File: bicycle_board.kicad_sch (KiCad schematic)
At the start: 70 parts, among them J1 Micro_SD_Card, J10 USB_A, J11 Conn_01x04, J12 Conn_01x01, J13 Conn_01x04, J14 Conn_01x01, J2 USB_C_Receptacle_USB2.0_16P, J5 Conn_01x08, J6 Conn_01x04, J7 Conn_01x05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

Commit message: 调整启动相关GPIO，ESO32添加GPIO9上拉电阻；STM32 BOOT0添加下拉电阻
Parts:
- added R6, R7: 10k, Resistor_SMD:R_0402_1005Metric, symbol Device:R
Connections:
- net +3.3V: now also R6.1
- net GND: now also R7.1
- net I2SO_BCK: now also U14.4 (IO5); no longer U14.7 (IO8)
- net I2SO_SD: now also U14.7 (IO8); no longer U14.8 (IO9)
- net I2SO_WS: now also U14.8 (IO9), R6.2; no longer U14.4 (IO5)
- net at U15.44 (BOOT0): now also R7.2
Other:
- note added: "GPIO2,8,9与启动模式有关"
- note added: "TF卡槽处已上拉"

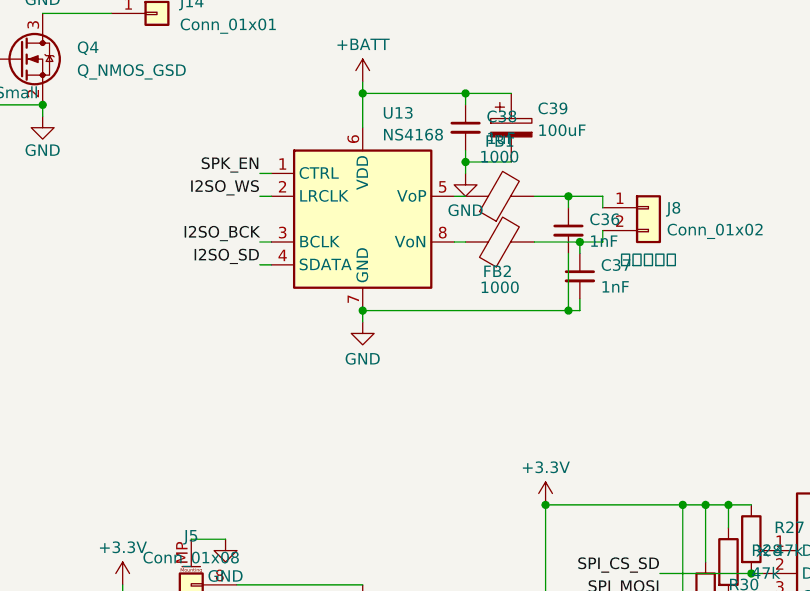
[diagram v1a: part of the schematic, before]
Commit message: 按数据手册调整NS4168布线，电源GND改用单点连接，加粗电源和喇叭走线到0.6mm，中心焊盘连接GND增强散热性能
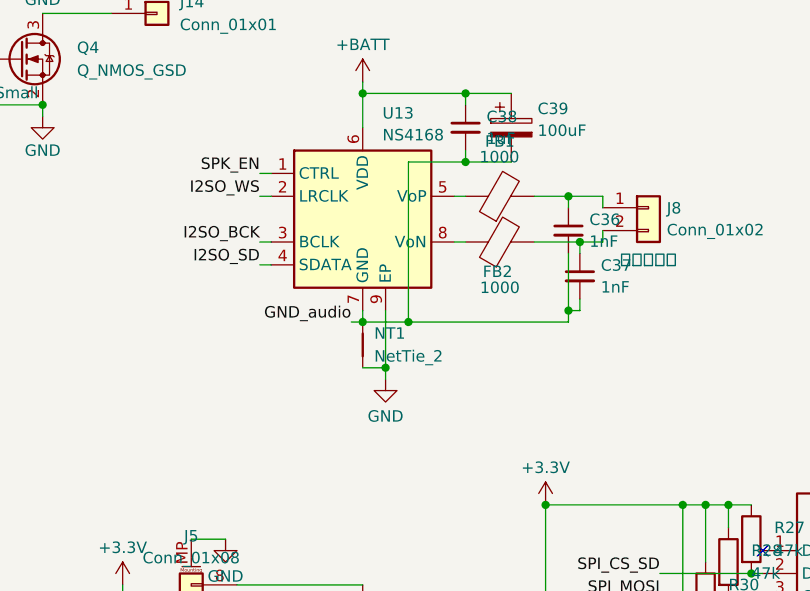
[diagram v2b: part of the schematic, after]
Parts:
- added NT1: NetTie_2, NetTie:NetTie-2_SMD_Pad0.5mm, symbol Device:NetTie_2
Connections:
- net GND: now also U13.9 (EP), NT1.1; no longer C36.2, C37.2, C38.2, C39.2, U13.7 (GND)
- new net GND_audio: C36.2, C37.2, C38.2, C39.2, NT1.2, U13.7 (GND)
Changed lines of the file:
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@@
 	)
 	(junction
+		(at 78.74 143.51)
+		(diameter 0)
+		(color 0 0 0 0)
+	)
+	(junction
 		(at 29.21 97.79)
 		(diameter 0)
@@
 	)
 	(junction
-		(at 73.66 142.24)
+		(at 93.98 176.53)
 		(diameter 0)
 		(color 0 0 0 0)
 	)
 	(junction
-		(at 93.98 176.53)
+		(at 115.57 63.5)
 		(diameter 0)
 		(color 0 0 0 0)
 	)
 	(junction
-		(at 115.57 63.5)
+		(at 232.41 118.11)
 		(diameter 0)
 		(color 0 0 0 0)
 	)
 	(junction
-		(at 232.41 118.11)
+		(at 76.2 148.59)
 		(diameter 0)
 		(color 0 0 0 0)
@@
 	)
 	(junction
-		(at 85.09 125.73)
-		(diameter 0)
-		(color 0 0 0 0)
-	)
-	(junction
 		(at 160.02 35.56)
 		(diameter 0)
@@
 	)
 	(junction
+		(at 85.09 125.73)
+		(diameter 0)
+		(color 0 0 0 0)
+	)
+	(junction
 		(at 161.29 35.56)
 		(diameter 0)
@@
 	)
 	(junction
-		(at 96.52 142.24)
+		(at 73.66 143.51)
 		(diameter 0)
 		(color 0 0 0 0)
@@
 	)
 	(junction
+		(at 96.52 142.24)
+		(diameter 0)
+		(color 0 0 0 0)
+	)
+	(junction
 		(at 265.43 148.59)
 		(diameter 0)
@@
 	(wire
 		(pts
+			(xy 72.39 143.51) (xy 73.66 143.51)
+		)
+		(stroke
+			(width 0)
+			(type default)
+		)
+	)
+	(wire
+		(pts
 			(xy 264.16 153.67) (xy 261.62 153.67)
 		)
@@
 	(wire
 		(pts
+			(xy 85.09 125.73) (xy 78.74 125.73)
+		)
+		(stroke
+			(width 0)
+			(type default)
+		)
+	)
+	(wire
+		(pts
 			(xy 170.18 26.67) (xy 170.18 27.94)
 		)
@@
 	(wire
 		(pts
+			(xy 73.66 143.51) (xy 78.74 143.51)
+		)
+		(stroke
+			(width 0)
+			(type default)
+		)
+	)
+	(wire
+		(pts
 			(xy 46.99 175.26) (xy 46.99 172.72)
 		)
@@
 	(wire
 		(pts
+			(xy 76.2 142.24) (xy 76.2 148.59)
+		)
+		(stroke
+			(width 0)
+			(type default)
+		)
+	)
+	(wire
+		(pts
 			(xy 257.81 104.14) (xy 259.08 104.14)
 		)
@@
 	(wire
 		(pts
+			(xy 73.66 142.24) (xy 73.66 143.51)
+		)
+		(stroke
+			(width 0)
+			(type default)
+		)
+	)
+	(wire
+		(pts
 			(xy 168.91 25.4) (xy 168.91 26.67)
 		)
@@
 	(wire
 		(pts
-			(xy 73.66 142.24) (xy 96.52 142.24)
-		)
-		(stroke
-			(width 0)
-			(type default)
-		)
-	)
-	(wire
-		(pts
 			(xy 222.25 115.57) (xy 222.25 128.27)
 		)
@@
 	(wire
 		(pts
+			(xy 76.2 148.59) (xy 73.66 148.59)
+		)
+		(stroke
+			(width 0)
+			(type default)
+		)
+	)
+	(wire
+		(pts
 			(xy 170.18 25.4) (xy 171.45 25.4)
 		)
@@
 	(wire
 		(pts
-			(xy 85.09 127) (xy 85.09 125.73)
-		)
-		(stroke
-			(width 0)
-			(type default)
-		)
-	)
-	(wire
-		(pts
 			(xy 96.52 129.54) (xy 100.33 129.54)
 		)
@@
 	(wire
 		(pts
+			(xy 76.2 149.86) (xy 76.2 148.59)
+		)
+		(stroke
+			(width 0)
+			(type default)
+		)
+	)
+	(wire
+		(pts
 			(xy 276.86 46.99) (xy 274.32 46.99)
 		)
@@
 	(wire
 		(pts
-			(xy 232.41 35.56) (xy 238.76 35.56)
+			(xy 96.52 143.51) (xy 96.52 142.24)
 		)
 		(stroke
@@
 	(wire
 		(pts
-			(xy 104.14 33.02) (xy 106.68 33.02)
+			(xy 232.41 35.56) (xy 238.76 35.56)
 		)
 		(stroke
@@
 	(wire
 		(pts
-			(xy 73.66 142.24) (xy 73.66 143.51)
+			(xy 104.14 33.02) (xy 106.68 33.02)
 		)
 		(stroke
@@
 	(wire
 		(pts
+			(xy 78.74 125.73) (xy 78.74 143.51)
+		)
+		(stroke
+			(width 0)
+			(type default)
+		)
+	)
+	(wire
+		(pts
 			(xy 160.02 35.56) (xy 161.29 35.56)
 		)
@@
 	(wire
 		(pts
+			(xy 78.74 143.51) (xy 96.52 143.51)
+		)
+		(stroke
+			(width 0)
+			(type default)
+		)
+	)
+	(wire
+		(pts
 			(xy 179.07 92.71) (xy 180.34 92.71)
 		)
@@
 		)
 	)
+	(label "GND_audio"
+		(at 72.39 143.51 180)
+		(fields_autoplaced yes)
+		(effects
+			(font
+				(size 1.27 1.27)
+			)
+			(justify right bottom)
+		)
+	)
 	(label "HALL2"
 		(at 276.86 31.75 0)
@@
 	(symbol
 		(lib_id "power:GND")
-		(at 85.09 127 0)
-		(unit 1)
-		(exclude_from_sim no)
-		(in_bom yes)
-		(on_board yes)
-		(dnp no)
-		(fields_autoplaced yes)
-		(property "Reference" "#PWR064"
-			(at 85.09 133.35 0)
-			(effects
-				(font
-					(size 1.27 1.27)
-				)
-				(hide yes)
-			)
-		)
-		(property "Value" "GND"
-			(at 85.09 131.1331 0)
-			(effects
-				(font
-					(size 1.27 1.27)
-				)
-			)
-		)
-		(property "Footprint" ""
-			(at 85.09 127 0)
-			(effects
-				(font
-					(size 1.27 1.27)
-				)
-				(hide yes)
-			)
-		)
-		(property "Datasheet" ""
-			(at 85.09 127 0)
-			(effects
-				(font
-					(size 1.27 1.27)
-				)
-				(hide yes)
-			)
-		)
-		(property "Description" "Power symbol creates a global label with name \"GND\" , ground"
-			(at 85.09 127 0)
-			(effects
-				(font
-					(size 1.27 1.27)
-				)
-				(hide yes)
-			)
-		)
-		(pin "1"
-		)
-		(instances
-			(project "bicycle_board"
-				(path "/a369956d-4c9f-46c3-810f-e3e9616ab1a2"
-					(reference "#PWR064")
-					(unit 1)
-				)
-			)
-		)
-	)
-	(symbol
-		(lib_id "power:GND")
 		(at 279.4 107.95 0)
 		(unit 1)
@@
 	(symbol
 		(lib_id "power:GND")
-		(at 73.66 143.51 0)
+		(at 76.2 149.86 0)
 		(unit 1)
 		(exclude_from_sim no)
@@
 		(fields_autoplaced yes)
 		(property "Reference" "#PWR043"
-			(at 73.66 149.86 0)
+			(at 76.2 156.21 0)
 			(effects
 				(font
@@
 		)
 		(property "Value" "GND"
-			(at 73.66 147.6431 0)
+			(at 76.2 153.9931 0)
 			(effects
 				(font
@@
 		)
 		(property "Footprint" ""
-			(at 73.66 143.51 0)
+			(at 76.2 149.86 0)
 			(effects
 				(font
@@
 		)
 		(property "Datasheet" ""
-			(at 73.66 143.51 0)
+			(at 76.2 149.86 0)
 			(effects
 				(font
@@
 		)
 		(property "Description" "Power symbol creates a global label with name \"GND\" , ground"
-			(at 73.66 143.51 0)
+			(at 76.2 149.86 0)
 			(effects
 				(font
@@
 		(pin "8"
 		)
+		(pin "9"
+		)
 		(instances
 			(project ""
@@
 					(unit 1)
 				)
+			)
+		)
+	)
+	(symbol
+		(lib_id "Device:NetTie_2")
+		(at 73.66 146.05 90)
+		(unit 1)
+		(exclude_from_sim no)
+		(in_bom no)
+		(on_board yes)
+		(dnp no)
+		(fields_autoplaced yes)
+		(property "Reference" "NT1"
+			(at 74.93 144.7799 90)
+			(effects
+				(font
+					(size 1.27 1.27)
+				)
+				(justify right)
+			)
+		)
+		(property "Value" "NetTie_2"
+			(at 74.93 147.3199 90)
+			(effects
+				(font
+					(size 1.27 1.27)
+				)
+				(justify right)
+			)
+		)
+		(property "Footprint" "NetTie:NetTie-2_SMD_Pad0.5mm"
+			(at 73.66 146.05 0)
+			(effects
+				(font
+					(size 1.27 1.27)
+				)
+				(hide yes)
+			)
+		)
+		(property "Datasheet" "~"
+			(at 73.66 146.05 0)
+			(effects
+				(font
+					(size 1.27 1.27)
+				)
+				(hide yes)
+			)
+		)
+		(property "Description" "Net tie, 2 pins"
+			(at 73.66 146.05 0)
+			(effects
+				(font
+					(size 1.27 1.27)
+				)
+				(hide yes)
+			)
+		)
+		(pin "2"
+		)
+		(pin "1"
+		)
+		(instances
+			(project ""
+				(path "/a369956d-4c9f-46c3-810f-e3e9616ab1a2"
+					(reference "NT1")
+					(unit 1)
+				)

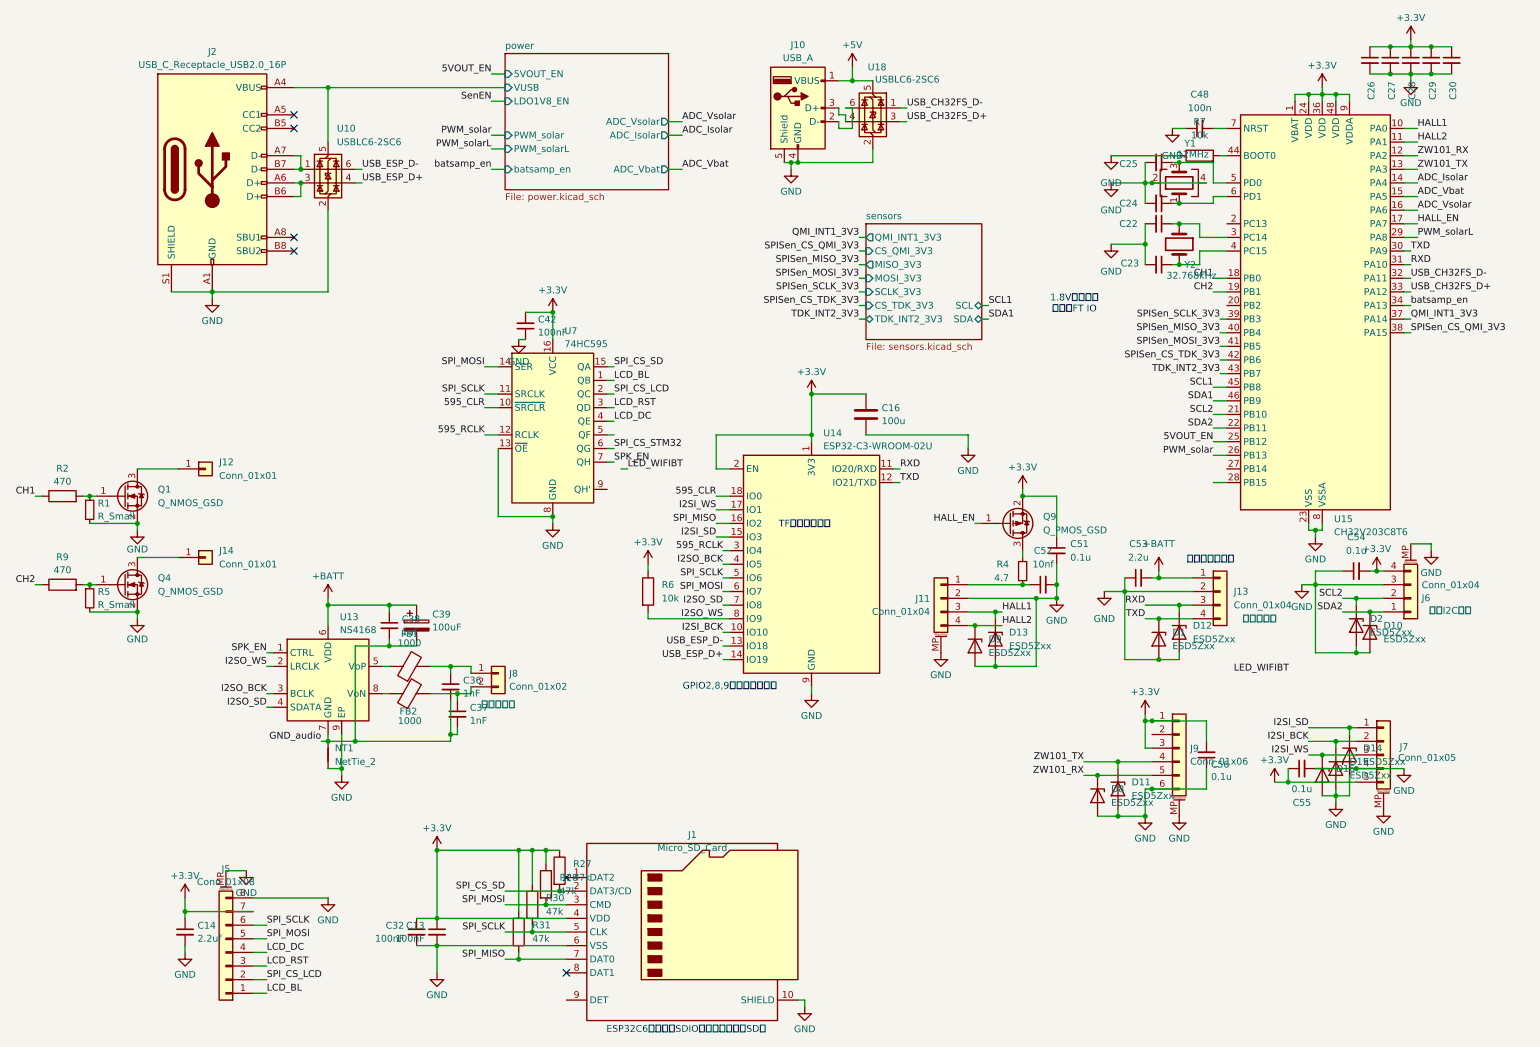
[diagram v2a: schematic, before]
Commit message: 修复一些ERC错误
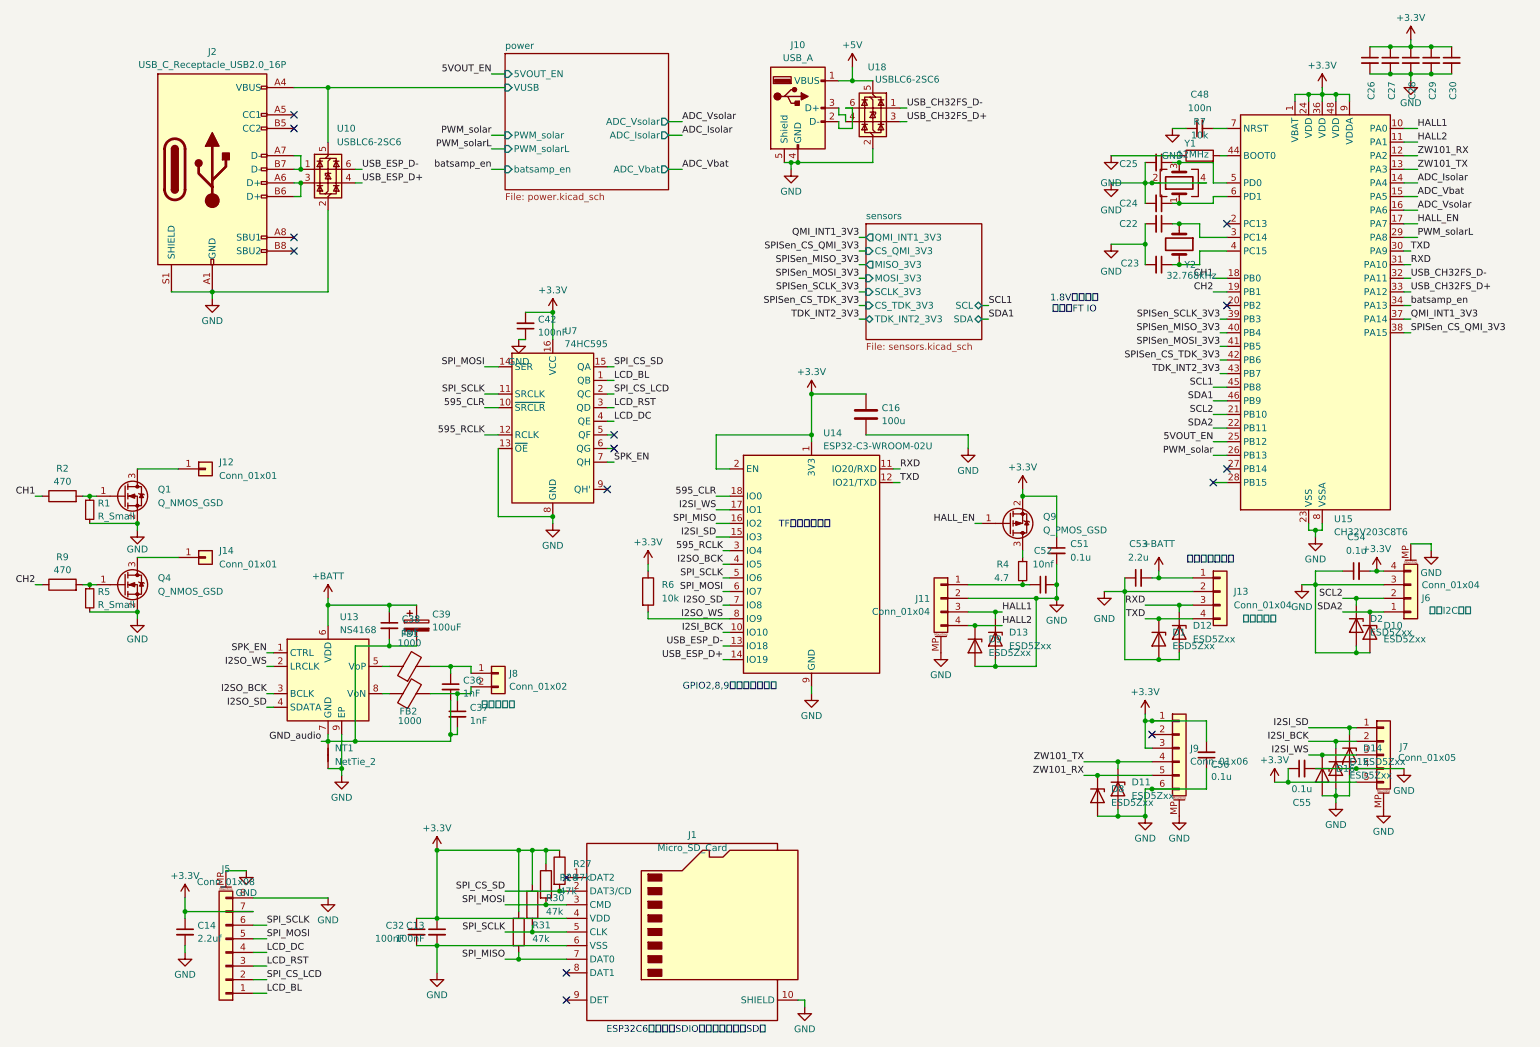
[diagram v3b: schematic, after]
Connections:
- net SPI_CS_STM32: no longer names the net of U7.6 (QG)
- no-connect marks 6 -> 15
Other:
- sheet power ports: added none; removed LDO1V8_EN
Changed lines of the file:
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@@
 	)
 	(no_connect
+		(at 238.76 95.25)
+	)
+	(no_connect
+		(at 227.33 142.24)
+	)
+	(no_connect
+		(at 118.11 191.77)
+	)
+	(no_connect
+		(at 127 86.36)
+	)
+	(no_connect
 		(at 67.31 26.67)
 	)
@@
 	)
 	(no_connect
+		(at 241.3 46.99)
+	)
+	(no_connect
+		(at 241.3 62.23)
+	)
+	(no_connect
 		(at 67.31 29.21)
 	)
 	(no_connect
+		(at 125.73 96.52)
+	)
+	(no_connect
+		(at 241.3 92.71)
+	)
+	(no_connect
+		(at 127 88.9)
+	)
+	(no_connect
 		(at 118.11 186.69)
 	)
@@
 	(wire
 		(pts
-			(xy 104.14 24.13) (xy 106.68 24.13)
-		)
-		(stroke
-			(width 0)
-			(type default)
-		)
-	)
-	(wire
-		(pts
 			(xy 222.25 115.57) (xy 234.95 115.57)
 		)
@@
 	(wire
 		(pts
-			(xy 129.54 92.71) (xy 128.27 92.71)
-		)
-		(stroke
-			(width 0)
-			(type default)
-		)
-	)
-	(wire
-		(pts
 			(xy 267.97 19.05) (xy 271.78 19.05)
 		)
@@
 		)
 	)
-	(label "LED_WIFIBT"
-		(at 129.54 92.71 0)
-		(fields_autoplaced yes)
-		(effects
-			(font
-				(size 1.27 1.27)
-			)
-			(justify left bottom)
-		)
-	)
 	(label "TXD"
 		(at 226.06 120.65 180)
@@
 		)
 	)
-	(label "SenEN"
-		(at 104.14 24.13 180)
-		(fields_autoplaced yes)
-		(effects
-			(font
-				(size 1.27 1.27)
-			)
-			(justify right bottom)
-		)
-	)
 	(label "USB_CH32FS_D-"
 		(at 181.61 25.4 0)
@@
 		)
 	)
-	(label "LED_WIFIBT"
-		(at 242.57 130.81 0)
-		(fields_autoplaced yes)
-		(effects
-			(font
-				(size 1.27 1.27)
-			)
-			(justify left bottom)
-		)
-	)
 	(label "I2SO_SD"
 		(at 147.32 118.11 180)
@@
 		)
 	)
-	(label "SPI_CS_STM32"
-		(at 127 88.9 0)
-		(fields_autoplaced yes)
-		(effects
-			(font
-				(size 1.27 1.27)
-			)
-			(justify left bottom)
-		)
-	)
 	(label "TXD"
 		(at 180.34 95.25 0)
@@
 			(effects
 				(font
-					(size 1.27 1.27)
-				)
-				(justify left)
-			)
-		)
-		(pin "LDO1V8_EN" input
-			(at 106.68 24.13 180)
-			(effects
-				(font
